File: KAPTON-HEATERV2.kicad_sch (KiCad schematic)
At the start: 26 parts, among them J1 XT60PW-M, J2 XT60PW-M, J3 1985276, J4 1985218, J5 10090926-P154XLF, K1 1-1393210-8, Q1 AO3400A, U1 TC4427ACOA, U2 INA181

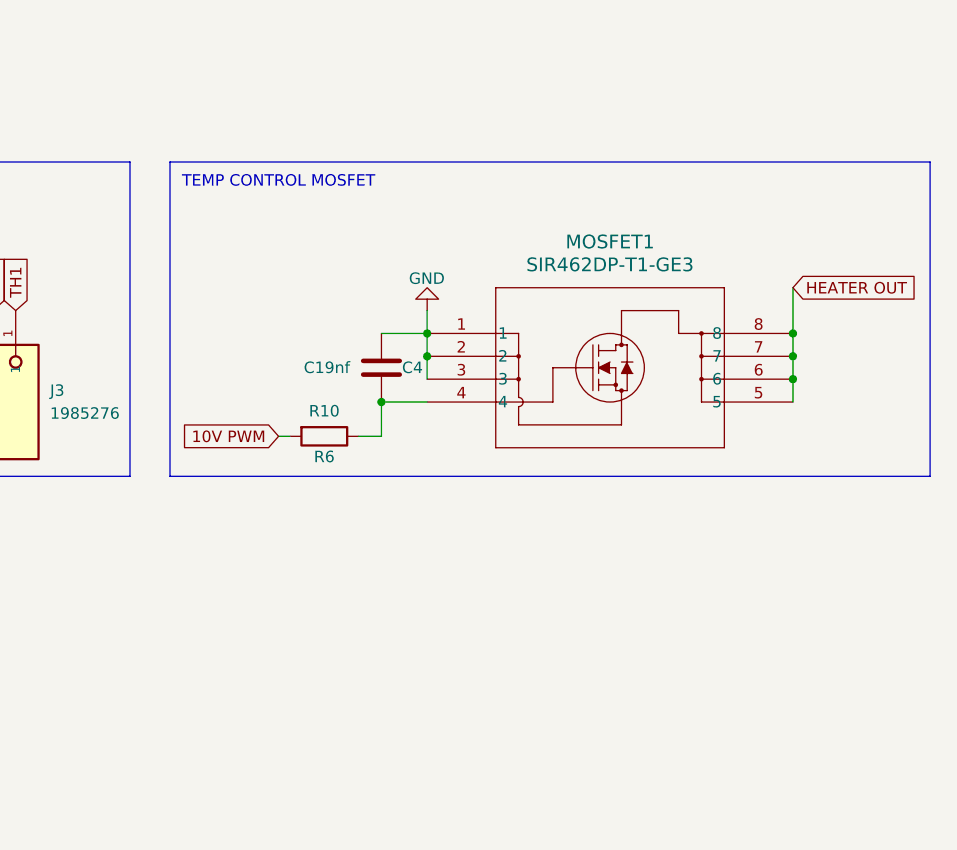
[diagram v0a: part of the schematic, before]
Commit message: added tvs diode
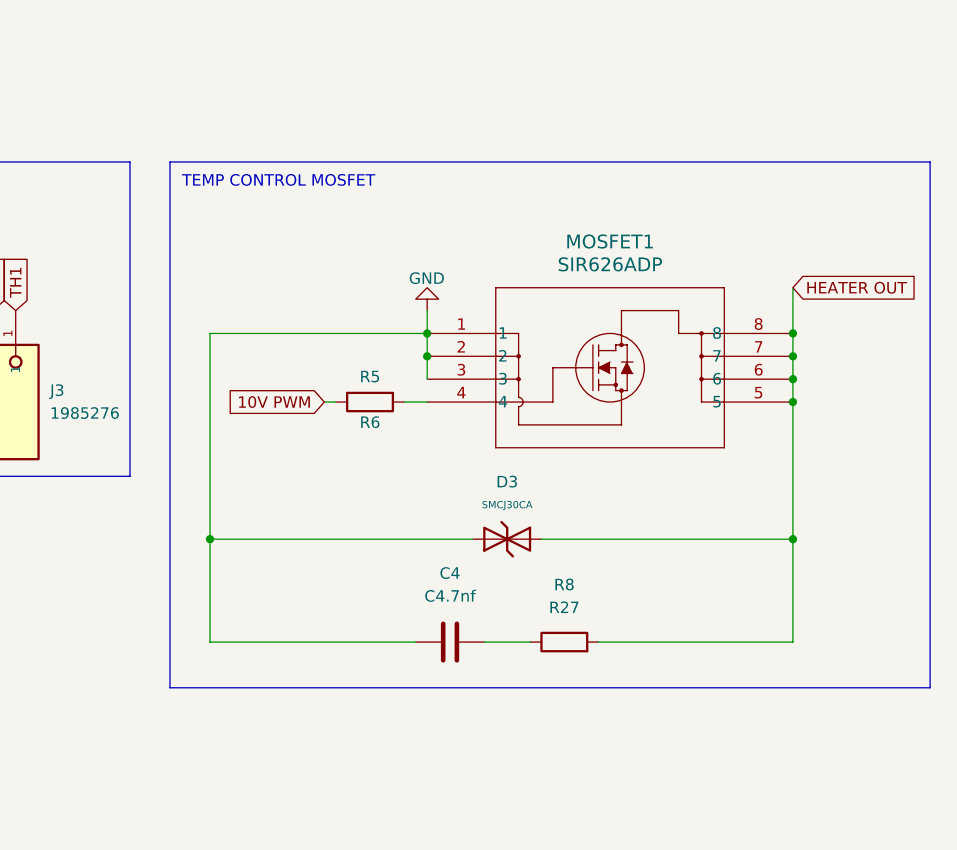
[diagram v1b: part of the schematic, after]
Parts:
- added D3: SMCJ30CA, PCM_JLCPCB:D_SMC, symbol PCM_JLCPCB-Diodes:TVS-Bi,SMCJ30CA
- added R8: R27, symbol Device:R
- C4: value C19nf -> C4.7nf; footprint Capacitor_SMD:C_0805_2012Metric -> (none)
- MOSFET1: value SIR462DP-T1-GE3 -> SIR626ADP
- R6: value R10 -> R5
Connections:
- net GND: now also D3.2
- net HEATER OUT: now also D3.1, R8.2
- net at MOSFET1.4, R6.1: no longer C4.1
- new net: C4.1, R8.1
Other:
- moved on the sheet: R6
